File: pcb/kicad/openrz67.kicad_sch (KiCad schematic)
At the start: 61 parts, among them J1 GPIO header, U1 ESP32-C3FH4, U2 TPS63031DSKR, U3 BQ25185DLHR, U4 S4B-XH-A(LF)(SN), U5 TLP172AM, U6 TLP172AM, X1 40MHz, X2 32.768kHz

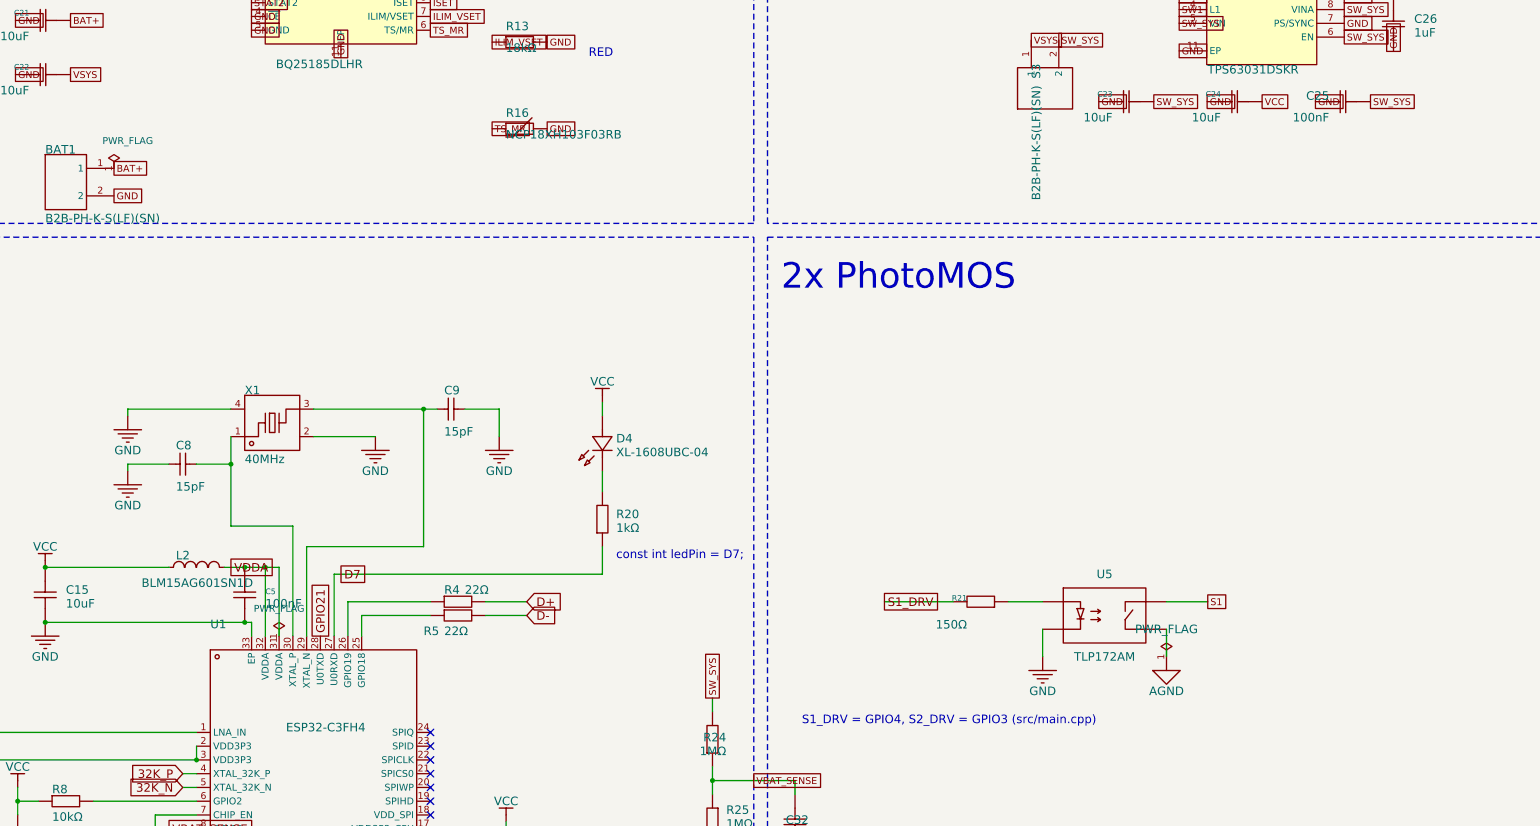
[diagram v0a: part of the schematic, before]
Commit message: PCB rev 3: reverse-battery P-FET Q3, C24 at the buck-boost output, EP paste windows, 0.8 mm RF line, review notes
Review round 2026-09-25 (pcb/kicad/notes/review-2026-09-25.md):
- Q3 AO3401A (SOT-23, C15127) between BAT1 pin 1 (new net BAT_CELL) and BAT+;
  gate to GND. VBUS moved to B.Cu under it; BAT+ rerouted west of L3 pad 1.
- C24 to (138.0, 97.0), 1.5 mm from U2 VOUT, with a return GND via.
- U1 exposed pad: no paste on the pad, four 1.5 mm aperture windows; U2/U3
  exposed pads 85 % paste. Same change in the library footprints.
- RF line 0.8 mm from the U.FL pad to C2 (~52 ohm).
- S2_DRV via 0.45/0.25 (no JLCPCB surcharge), nudged into the free slot.
- Bottom silk v3, '+' at BAT1 pin 1, schematic note for rev 3 pins.
- README: rev 3 section, accepted warnings (13 courtyard), fab notes, the
  findings accepted without a change and why.
DRC 0 errors / 16 warnings, ERC 0 errors / 15 warnings, parity clean.
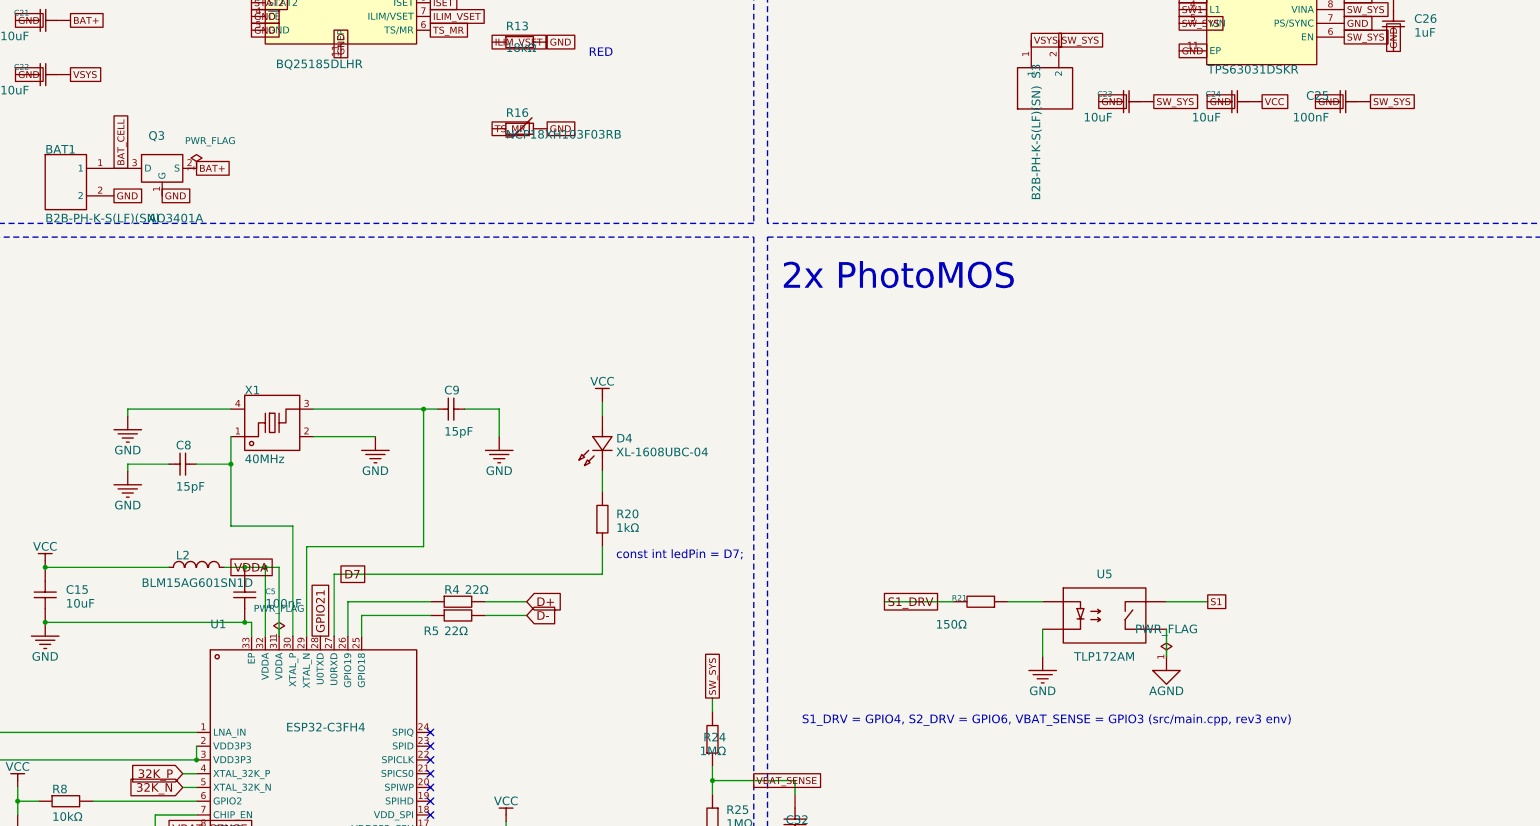
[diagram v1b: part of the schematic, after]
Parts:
- added Q3: AO3401A, openrz67:SOT-23, symbol openrz67:AO3401A
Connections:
- net BAT+: now also Q3.2 (S); no longer BAT1.1
- net GND: now also Q3.1 (G)
- new net BAT_CELL: BAT1.1, Q3.3 (D)
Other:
- note added: "S1_DRV = GPIO4, S2_DRV = GPIO6, VBAT_SENSE = GPIO3 (src/main.cpp, rev3 env)"
- note removed: "S1_DRV = GPIO4, S2_DRV = GPIO3 (src/main.cpp)"
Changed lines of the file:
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@@
     (effects (font (size 4.7244 4.7244)) (justify left bottom))
   )
-  (text "S1_DRV = GPIO4, S2_DRV = GPIO3 (src/main.cpp)" (at 245.11 170.18 0)
+  (text "S1_DRV = GPIO4, S2_DRV = GPIO6, VBAT_SENSE = GPIO3 (src/main.cpp, rev3 env)" (at 245.11 170.18 0)
     (effects (font (size 1.5748 1.5748)) (justify left bottom))
   )
@@
     (effects (font (size 1.27 1.27)) (justify left bottom))
   )
-  (global_label "BAT+" (shape passive) (at 118.11 67.31 0)
+  (global_label "BAT+" (shape passive) (at 133.35 67.31 0)
     (effects (font (size 1.27 1.27)) (justify left bottom))
   )
@@
     )
   )
+  (symbol (lib_id "openrz67:AO3401A") (at 127 67.31 0) (unit 1)
+    (in_bom yes) (on_board yes) (dnp no)
+    (property "Reference" "Q3" (at 124.46 62.23 0)
+      (effects (font (size 1.5748 1.5748)) (justify left bottom))
+    )
+    (property "Value" "AO3401A" (at 124.46 77.47 0)
+      (effects (font (size 1.5748 1.5748)) (justify left bottom))
+    )
+    (property "Footprint" "openrz67:SOT-23" (at 127 67.31 0)
+      (effects (font (size 1.27 1.27)) hide)
+    )
+    (property "Datasheet" "https://www.lcsc.com/product-detail/C15127.html" (at 127 67.31 0)
+      (effects (font (size 1.27 1.27)) hide)
+    )
+    (property "Description" "Reverse-battery block: D to the cell, S to BAT+, G to GND" (at 127 67.31 0)
+      (effects (font (size 1.27 1.27)) hide)
+    )
+    (property "Manufacturer Part" "AO3401A" (at 127 67.31 0)
+      (effects (font (size 1.27 1.27)) hide)
+    )
+    (property "Manufacturer" "Alpha & Omega Semicon" (at 127 67.31 0)
+      (effects (font (size 1.27 1.27)) hide)
+    )
+    (property "Supplier Part" "C15127" (at 127 67.31 0)
+      (effects (font (size 1.27 1.27)) hide)
+    )
+    (property "Supplier" "LCSC" (at 127 67.31 0)
+      (effects (font (size 1.27 1.27)) hide)
+    )
+    (pin "1")
+    (pin "2")
+    (pin "3")
+    (instances
+      (project "openrz67"
+        (path "/608428cc-ede5-4359-a9e7-0ca7713b40fb"
+          (reference "Q3") (unit 1)
+        )
+      )
+    )
+  )
+  (wire (pts (xy 118.11 67.31) (xy 120.65 67.31))
+    (stroke (width 0) (type default))
+  )
+  (global_label "BAT_CELL" (shape passive) (at 119.38 67.31 90)
+    (effects (font (size 1.27 1.27)) (justify left bottom))
+  )
+  (global_label "GND" (shape passive) (at 127 72.39 0)
+    (effects (font (size 1.27 1.27)) (justify left bottom))
+  )
   (symbol (lib_id "openrz67:U.FL-R-SMT-1(80)") (at 29.21 142.24 90) (unit 1)
     (in_bom yes) (on_board yes) (dnp no)
@@
     )
   )
-  (symbol (lib_id "openrz67:PWR_FLAG") (at 118.11 67.31 0) (unit 1)
+  (symbol (lib_id "openrz67:PWR_FLAG") (at 133.35 67.31 0) (unit 1)
     (in_bom yes) (on_board yes) (dnp no)
-    (property "Reference" "#FLG04" (at 118.11 63.5 0)
+    (property "Reference" "#FLG04" (at 133.35 63.5 0)
       (effects (font (size 1.27 1.27)) hide)
     )
-    (property "Value" "PWR_FLAG" (at 120.65 62.230000000000004 0)
+    (property "Value" "PWR_FLAG" (at 135.89 62.230000000000004 0)
       (effects (font (size 1.27 1.27)))
     )
-    (property "Footprint" "" (at 118.11 67.31 0)
+    (property "Footprint" "" (at 133.35 67.31 0)
       (effects (font (size 1.27 1.27)) hide)
     )
-    (property "Datasheet" "~" (at 118.11 67.31 0)
+    (property "Datasheet" "~" (at 133.35 67.31 0)
       (effects (font (size 1.27 1.27)) hide)
     )
-    (property "Description" "" (at 118.11 67.31 0)
+    (property "Description" "" (at 133.35 67.31 0)
       (effects (font (size 1.27 1.27)) hide)
     )
